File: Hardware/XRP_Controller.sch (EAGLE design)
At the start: 125 parts, among them J1 POWER_JACKPOWER_JACK_SLOT, J12 Vertical Qwiic Connector, J13 Vertical Qwiic Connector, J14 Vertical Qwiic Connector, J3 JST_6_PIN_VERTICAL, J4 JST_6_PIN_VERTICAL, J5 JST_6_PIN_VERTICAL, J6 JST_6_PIN_VERTICAL, J9 Vertical Qwiic Connector, Q3 20V/4.2A/52mΩ/1.4W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

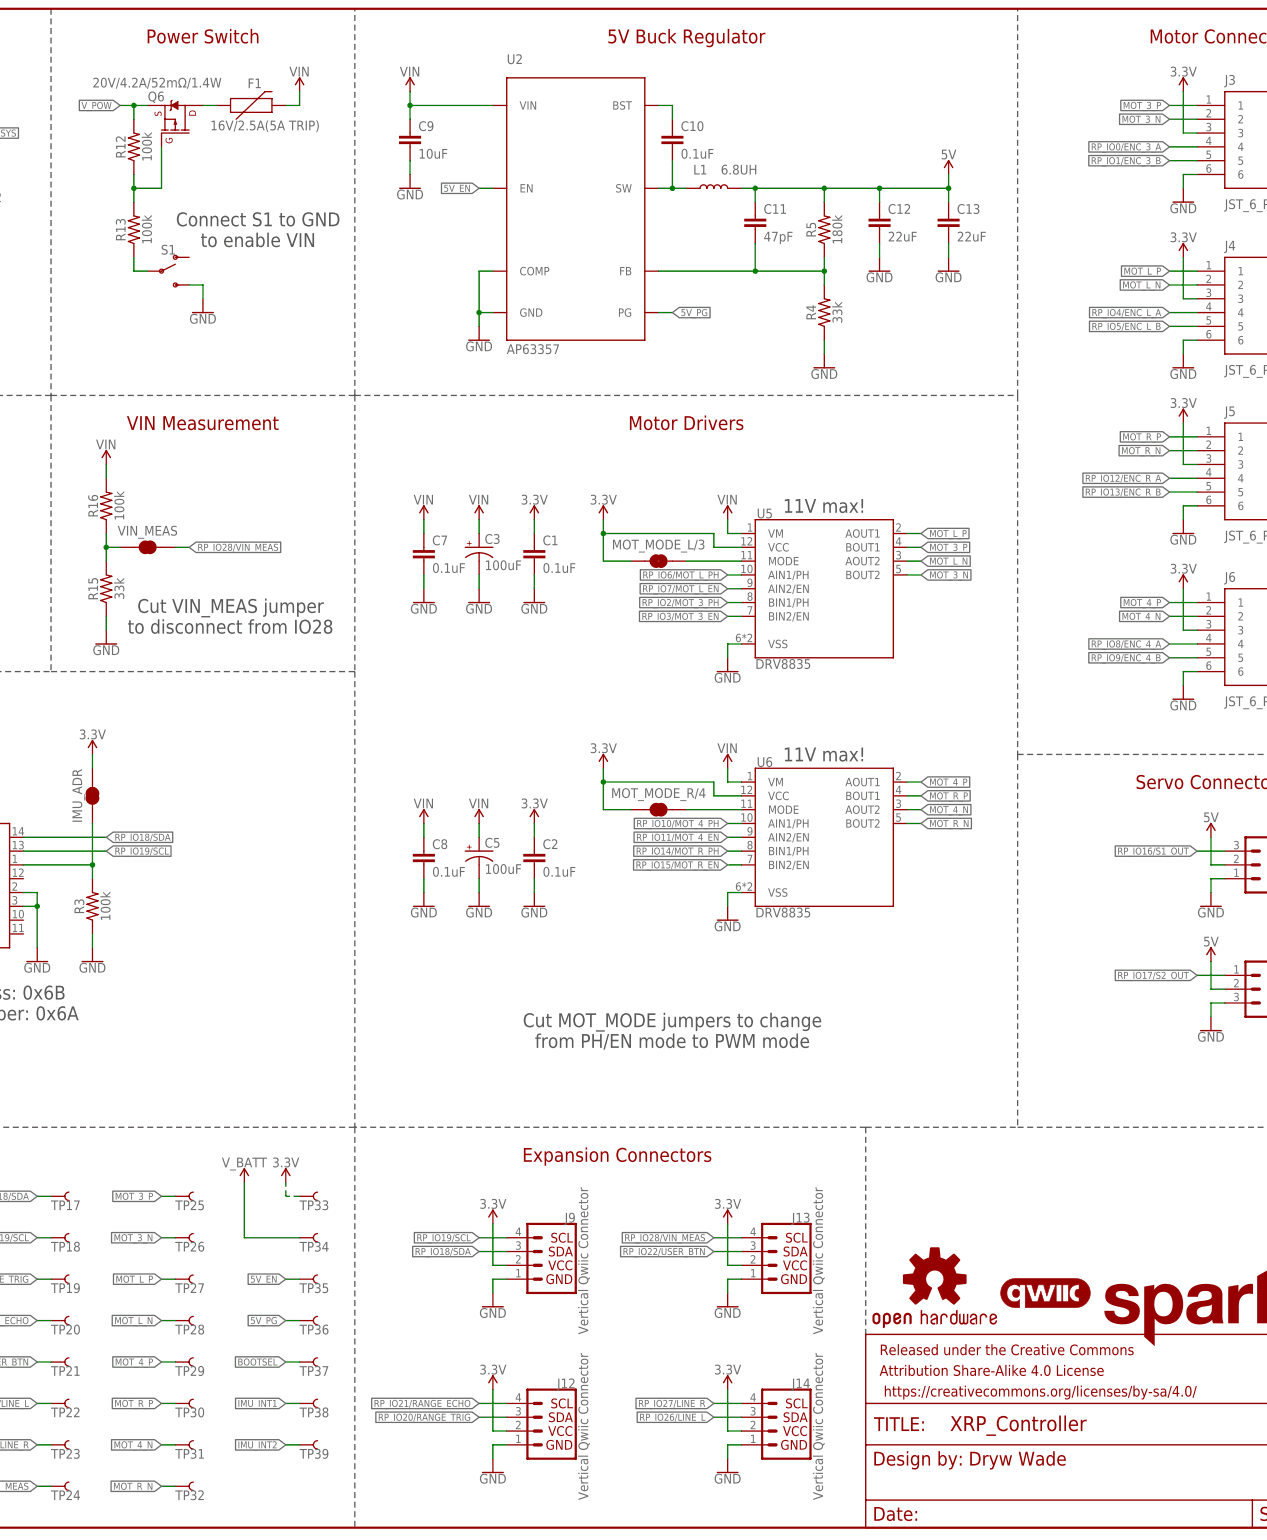
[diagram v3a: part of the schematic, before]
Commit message: Minor tweaks
Update buck footprint to link to SFE Eagle library
Change motor nets and silk labels to use +/- instead of P/N
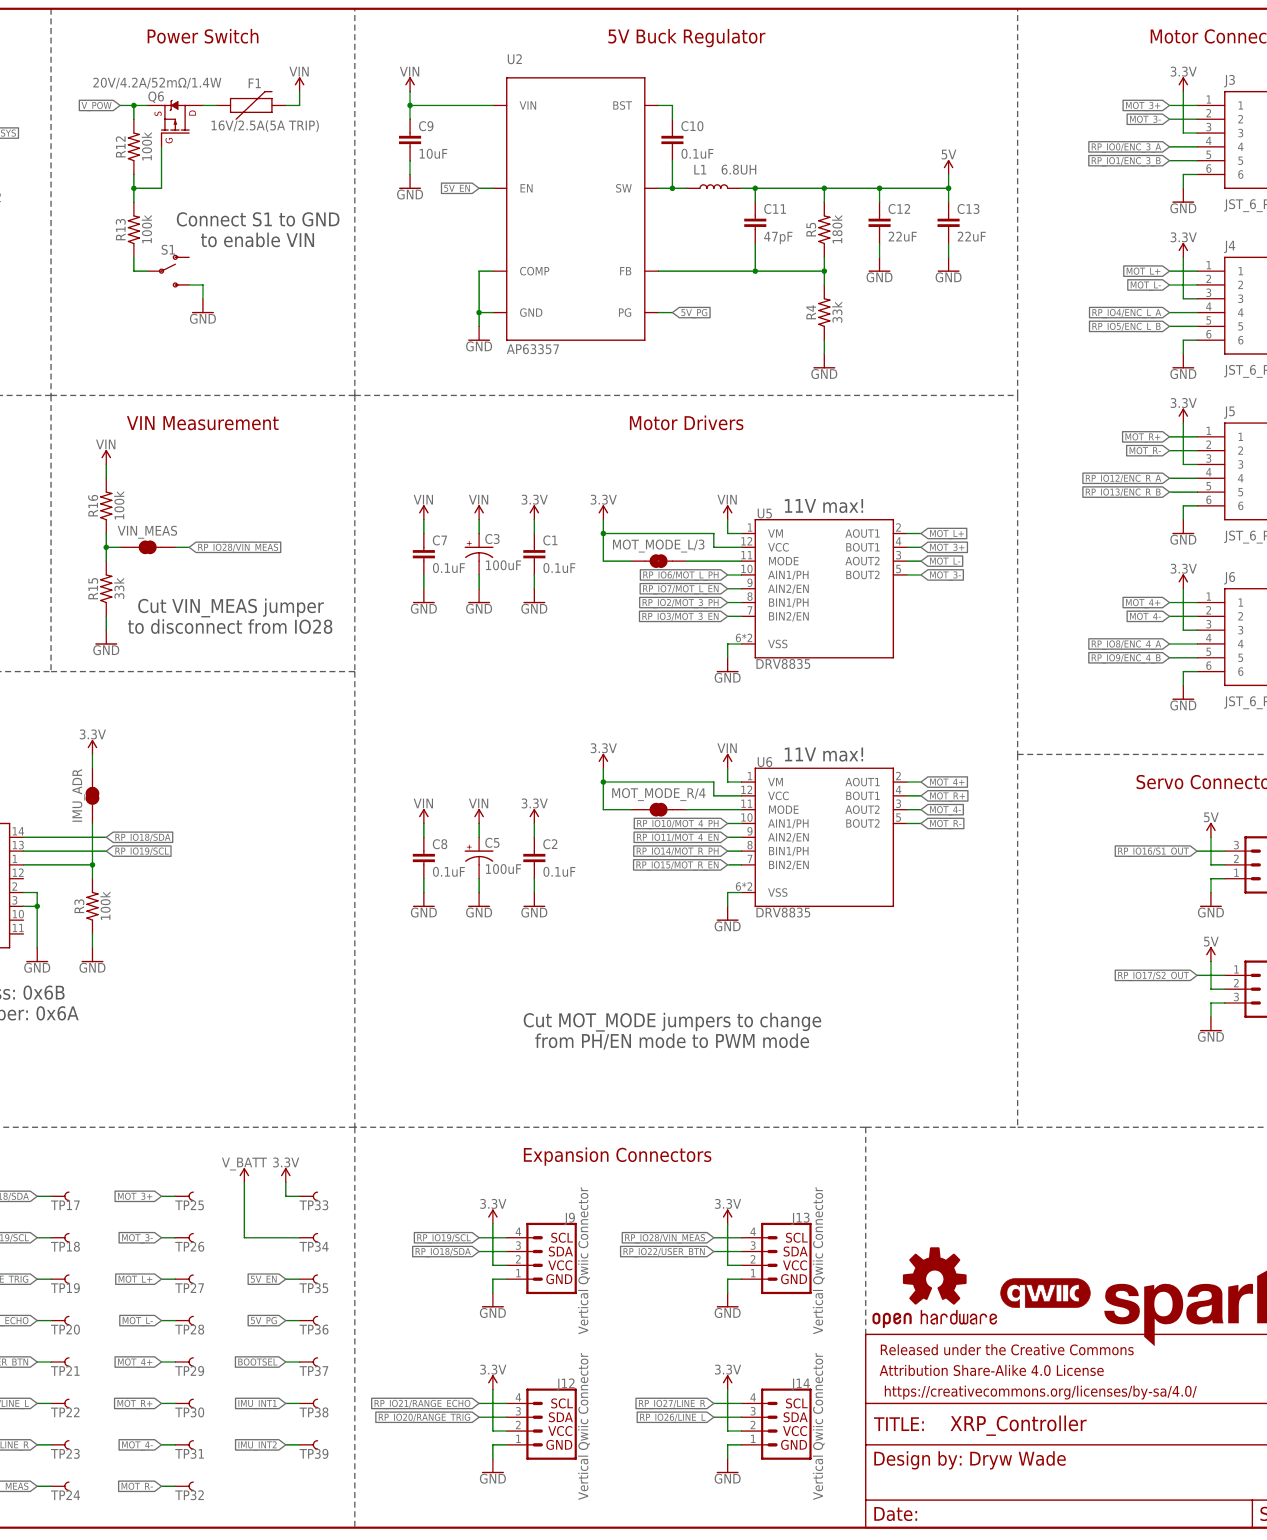
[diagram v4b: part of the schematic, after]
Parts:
- U2: device Buck5V:AP63357 -> SparkFun-IC-Power:AP63357
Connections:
- net MOT_3_N renamed MOT_3-
- net MOT_3_P renamed MOT_3+
- net MOT_4_N renamed MOT_4-
- net MOT_4_P renamed MOT_4+
- net MOT_L_N renamed MOT_L-
- net MOT_L_P renamed MOT_L+
- net MOT_R_N renamed MOT_R-
- net MOT_R_P renamed MOT_R+
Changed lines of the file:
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@@
 <part name="SUPPLY18" library="SparkFun-PowerSymbols" deviceset="5V" device=""/>
 <part name="SUPPLY19" library="SparkFun-PowerSymbols" deviceset="5V" device=""/>
-<part name="U2" library="Buck5V" deviceset="AP63357" device="" value="AP63357"/>
+<part name="U2" library="SparkFun-IC-Power" deviceset="AP63357" device="" value="AP63357"/>
 <part name="C9" library="SparkFun-Capacitors" deviceset="10UF" device="-0805-25V-10%" value="10uF"/>
 <part name="GND16" library="SparkFun-PowerSymbols" deviceset="GND" device=""/>
@@
 <pinref part="TP33" gate="G$1" pin="1"/>
 <pinref part="SUPPLY28" gate="G$1" pin="3.3V"/>
-<wire x1="226.06" y1="60.96" x2="223.52" y2="60.96" width="0.1524" layer="91" style="longdash"/>
-<wire x1="223.52" y1="60.96" x2="223.52" y2="63.5" width="0.1524" layer="91" style="longdash"/>
+<wire x1="226.06" y1="60.96" x2="223.52" y2="60.96" width="0.1524" layer="91"/>
+<wire x1="223.52" y1="60.96" x2="223.52" y2="63.5" width="0.1524" layer="91"/>
 </segment>
 <segment>
@@
 </segment>
 </net>
-<net name="MOT_3_P" class="0">
+<net name="MOT_3+" class="0">
 <segment>
 <wire x1="391.16" y1="261.62" x2="386.08" y2="261.62" width="0.1524" layer="91"/>
@@
 </segment>
 </net>
-<net name="MOT_3_N" class="0">
+<net name="MOT_3-" class="0">
 <segment>
 <wire x1="391.16" y1="259.08" x2="386.08" y2="259.08" width="0.1524" layer="91"/>
@@
 </segment>
 </net>
-<net name="MOT_L_P" class="0">
+<net name="MOT_L+" class="0">
 <segment>
 <wire x1="391.16" y1="231.14" x2="386.08" y2="231.14" width="0.1524" layer="91"/>
@@
 </segment>
 </net>
-<net name="MOT_L_N" class="0">
+<net name="MOT_L-" class="0">
 <segment>
 <wire x1="391.16" y1="228.6" x2="386.08" y2="228.6" width="0.1524" layer="91"/>
@@
 </segment>
 </net>
-<net name="MOT_R_P" class="0">
+<net name="MOT_R+" class="0">
 <segment>
 <wire x1="391.16" y1="200.66" x2="386.08" y2="200.66" width="0.1524" layer="91"/>
@@
 </segment>
 </net>
-<net name="MOT_R_N" class="0">
+<net name="MOT_R-" class="0">
 <segment>
 <wire x1="391.16" y1="198.12" x2="386.08" y2="198.12" width="0.1524" layer="91"/>
@@
 </segment>
 </net>
-<net name="MOT_4_P" class="0">
+<net name="MOT_4+" class="0">
 <segment>
 <wire x1="391.16" y1="170.18" x2="386.08" y2="170.18" width="0.1524" layer="91"/>
@@
 </segment>
 </net>
-<net name="MOT_4_N" class="0">
+<net name="MOT_4-" class="0">
 <segment>
 <wire x1="391.16" y1="167.64" x2="386.08" y2="167.64" width="0.1524" layer="91"/>
